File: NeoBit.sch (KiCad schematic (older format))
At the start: 18 parts, among them J2 Barrel_Jack_MountingPin, J5 microbit_edge_connector, U1 74AHCT125, U2 MCP1702-3302E_TO92

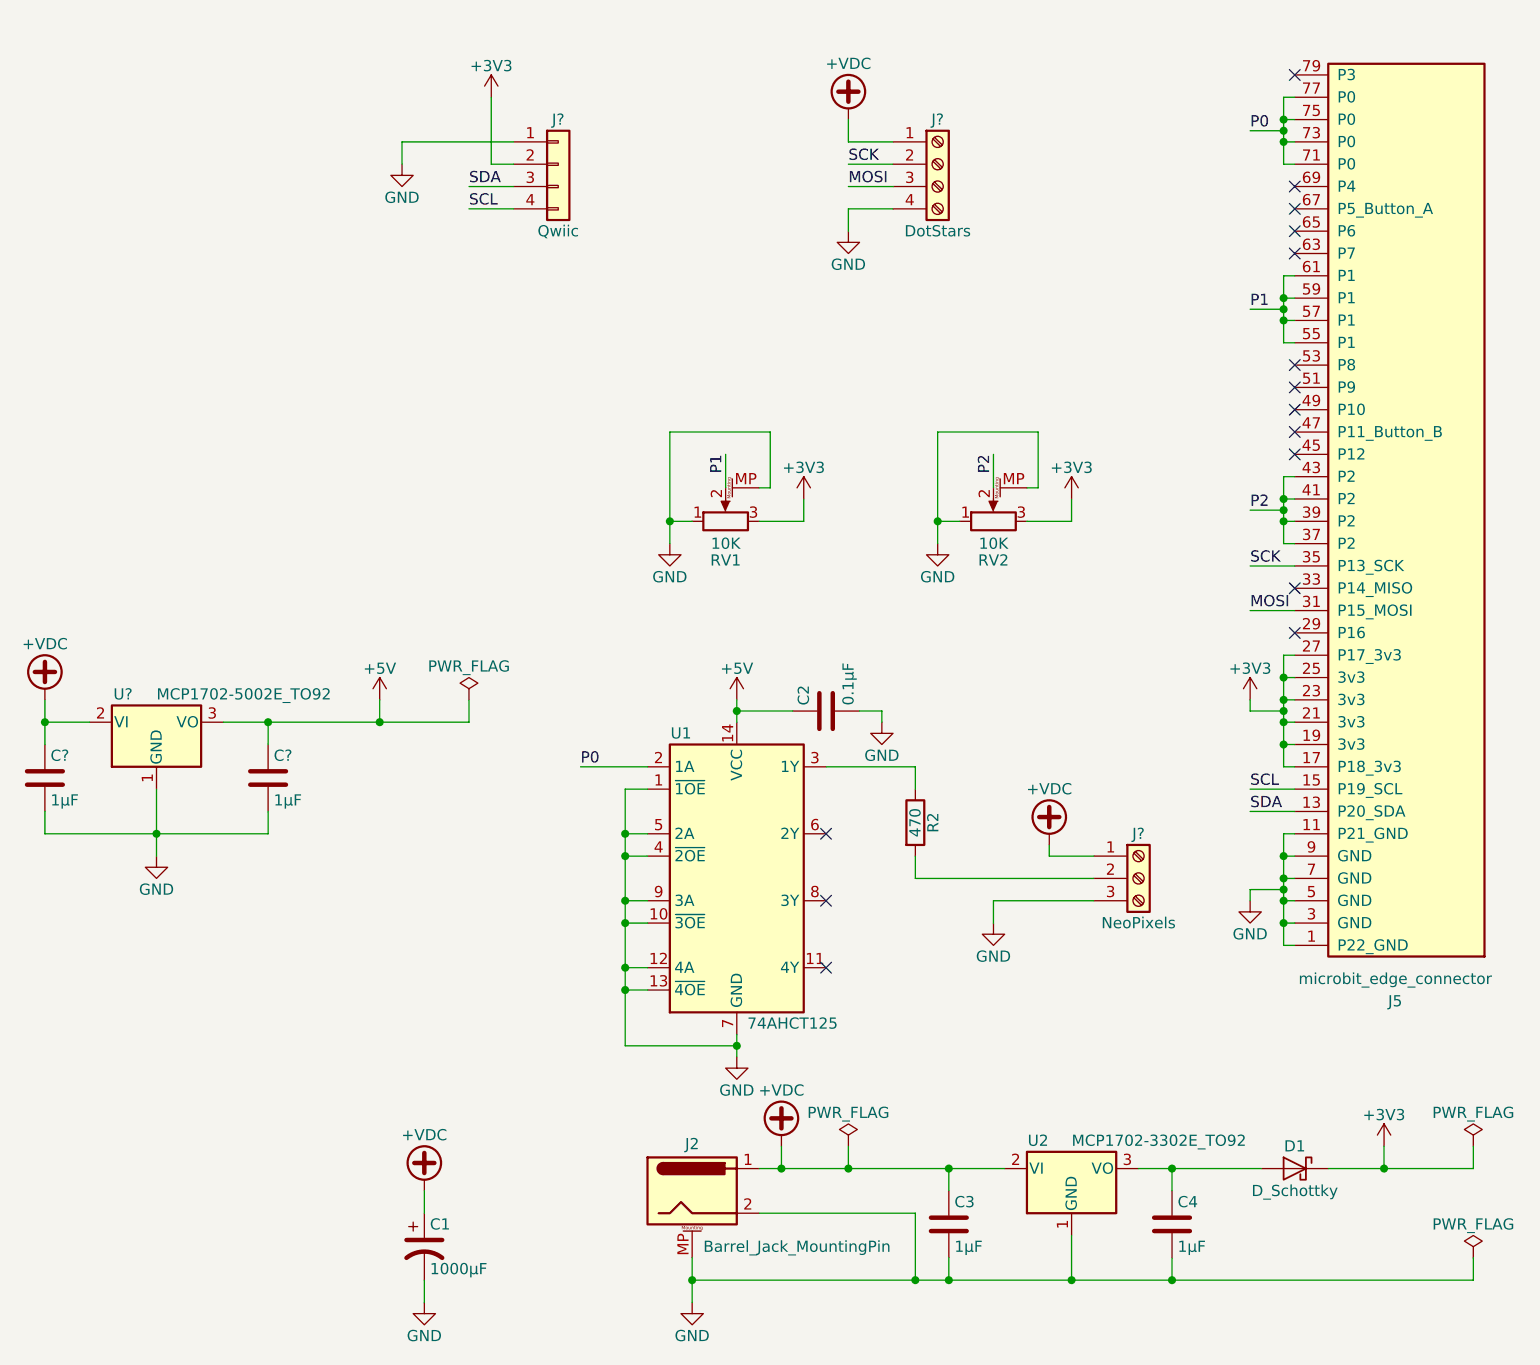
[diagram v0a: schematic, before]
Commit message: Put audio jack on P0; move NeoPixels to P16.
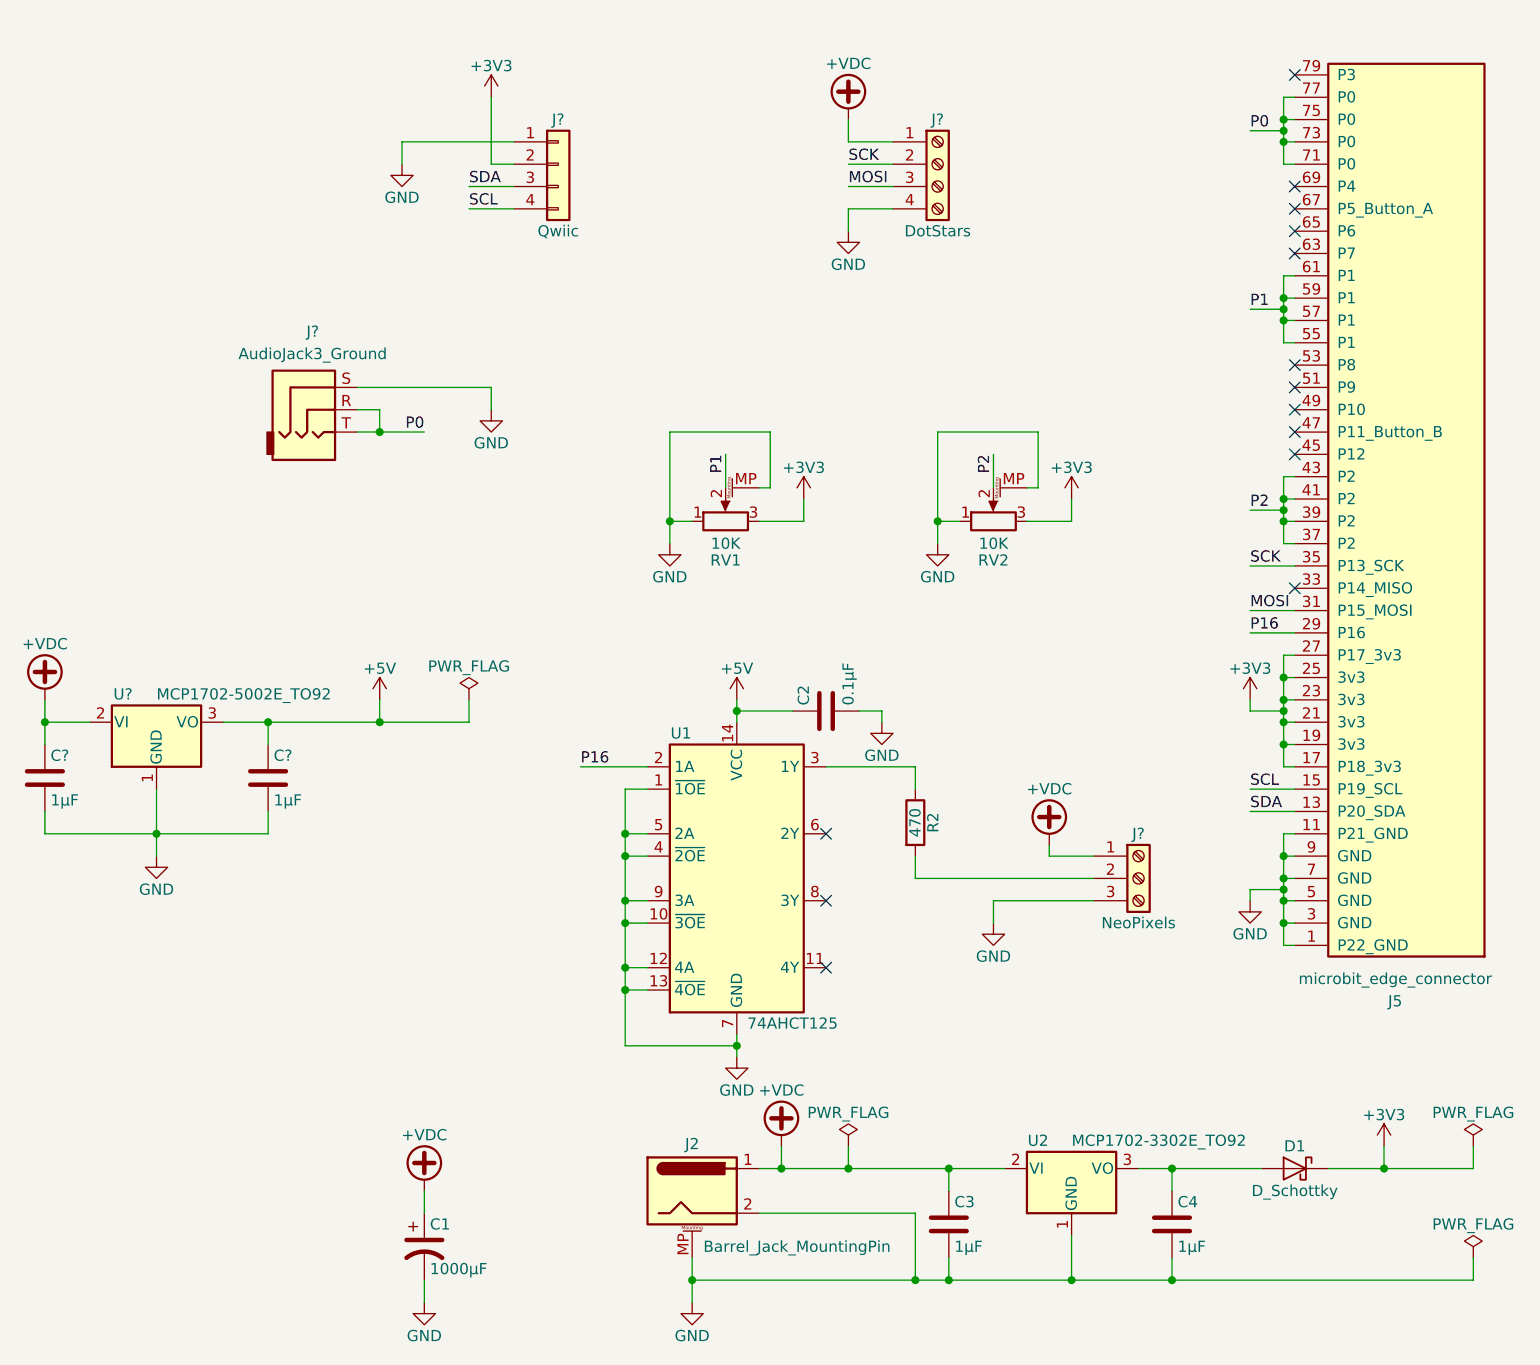
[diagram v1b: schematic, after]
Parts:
- added J?: AudioJack3_Ground, symbol AudioJack3_Ground
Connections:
- net GND: now also J?.S
- net P0: now also J?.R, J?.T; no longer U1.2 (1A)
- net P16: now reaches J5.29 (P16)
- net P16: now also U1.2 (1A)
- no-connect marks 15 -> 14
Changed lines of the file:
@@
 Connection ~ 4200 5300
 Text Label 4000 4300 0    50   ~ 0
-P0
+P16
 Wire Wire Line
 	4000 4300 4300 4300
@@
 NoConn ~ 7200 2900
 NoConn ~ 7200 3500
-NoConn ~ 7200 3700
 Wire Wire Line
 	7600 6000 7600 6100
@@
 Wire Wire Line
 	3500 1800 3700 1800
+$Comp
+L AudioJack3_Ground J?
+U 1 1 5BA405B2
+P 2800 2700
+F 0 "J?" H 2800 3050 50  0000 C CNN
+F 1 "AudioJack3_Ground" H 2800 2950 50  0000 C CNN
+F 2 "" H 2800 2700 50  0001 C CNN
+F 3 "" H 2800 2700 50  0001 C CNN
+	1    2800 2700
+	1    0    0    -1
+$EndComp
+$Comp
+L GND #PWR?
+U 1 1 5BA40629
+P 3600 2700
+F 0 "#PWR?" H 3600 2450 50  0001 C CNN
+F 1 "GND" H 3600 2550 50  0000 C CNN
+F 2 "" H 3600 2700 50  0001 C CNN
+F 3 "" H 3600 2700 50  0001 C CNN
+	1    3600 2700
+	1    0    0    -1
+$EndComp
+Wire Wire Line
+	3000 2600 3600 2600
+Wire Wire Line
+	3600 2600 3600 2700
+Text Label 3300 2800 2    50   ~ 0
+P0
+Wire Wire Line
+	3000 2800 3300 2800
+Wire Wire Line
+	3000 2700 3100 2700
+Wire Wire Line
+	3100 2700 3100 2800
+Connection ~ 3100 2800
+Text Label 7000 3700 0    50   ~ 0
+P16
+Wire Wire Line
+	7000 3700 7200 3700
 $EndSCHEMATC

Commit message: Annotate schematic.
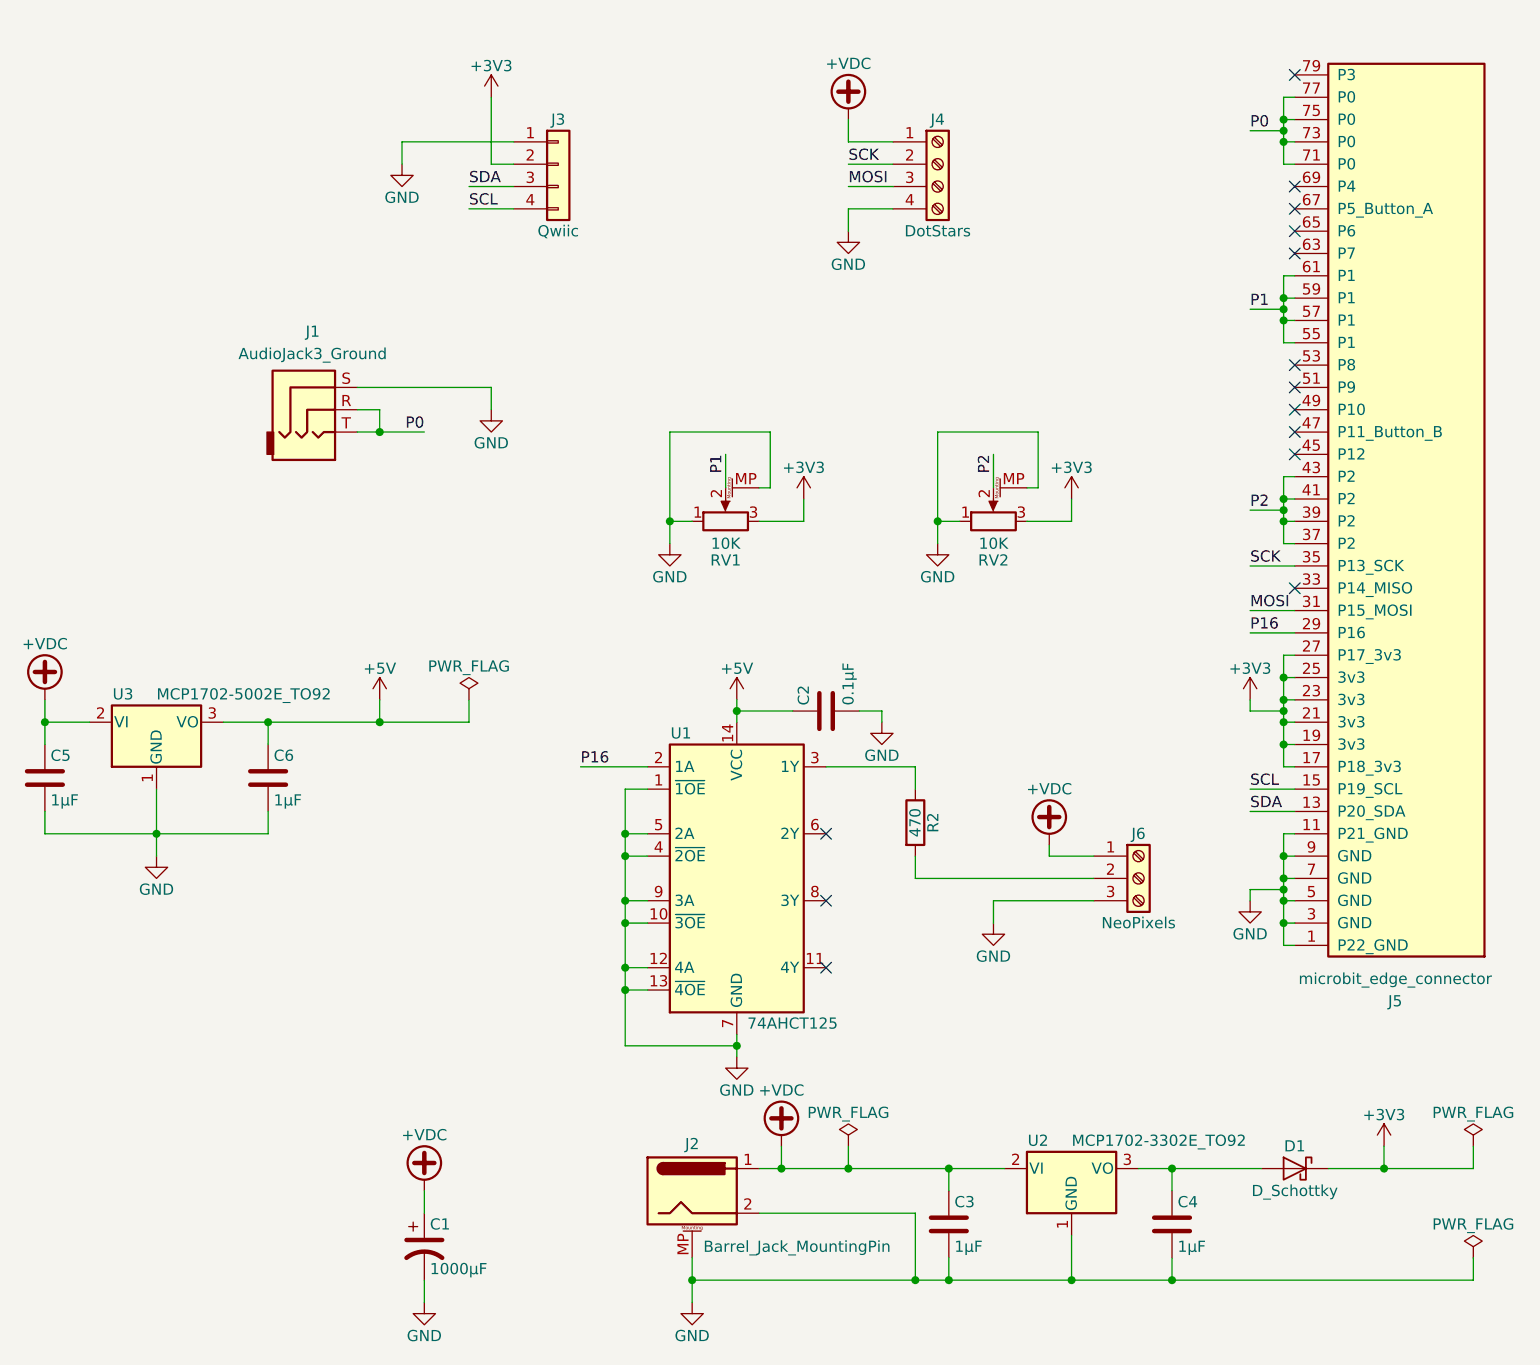
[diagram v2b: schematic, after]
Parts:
- J1: renamed from J?; Description (none) -> CONN JACK STEREO 3.5MM R/A; Digi-Key_PN (none) -> CP1-3523N-ND; MPN (none) -> SJ1-3523N
- gave numbers to parts that had none: 6
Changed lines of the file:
@@
 	4700 5500 4700 5600
 $Comp
-L GND #PWR08
+L GND #PWR07
 U 1 1 5B879F3C
 P 4500 6700
-F 0 "#PWR08" H 4500 6450 50  0001 C CNN
+F 0 "#PWR07" H 4500 6450 50  0001 C CNN
 F 1 "GND" H 4500 6550 50  0000 C CNN
 F 2 "" H 4500 6700 50  0001 C CNN
@@
 Connection ~ 6200 6600
 $Comp
-L +3V3 #PWR09
+L +3V3 #PWR08
 U 1 1 5B87BEFA
 P 7600 6000
-F 0 "#PWR09" H 7600 5850 50  0001 C CNN
+F 0 "#PWR08" H 7600 5850 50  0001 C CNN
 F 1 "+3V3" H 7600 6140 50  0000 C CNN
 F 2 "" H 7600 6000 50  0001 C CNN
@@
 $EndComp
 $Comp
-L GND #PWR010
+L GND #PWR09
 U 1 1 5B87CC46
 P 5350 4100
-F 0 "#PWR010" H 5350 3850 50  0001 C CNN
+F 0 "#PWR09" H 5350 3850 50  0001 C CNN
 F 1 "GND" H 5350 3950 50  0000 C CNN
 F 2 "" H 5350 4100 50  0001 C CNN
@@
 $EndComp
 $Comp
-L GND #PWR011
+L GND #PWR010
 U 1 1 5B87D3B2
 P 3300 6700
-F 0 "#PWR011" H 3300 6450 50  0001 C CNN
+F 0 "#PWR010" H 3300 6450 50  0001 C CNN
 F 1 "GND" H 3300 6550 50  0000 C CNN
 F 2 "" H 3300 6700 50  0001 C CNN
@@
 	3300 6600 3300 6700
 $Comp
-L PWR_FLAG #FLG013
+L PWR_FLAG #FLG011
 U 1 1 5B87DB70
 P 5200 6000
-F 0 "#FLG013" H 5200 6075 50  0001 C CNN
+F 0 "#FLG011" H 5200 6075 50  0001 C CNN
 F 1 "PWR_FLAG" H 5200 6150 50  0000 C CNN
 F 2 "" H 5200 6000 50  0001 C CNN
@@
 $EndComp
 $Comp
-L PWR_FLAG #FLG014
+L PWR_FLAG #FLG012
 U 1 1 5B87DBB4
 P 8000 6000
-F 0 "#FLG014" H 8000 6075 50  0001 C CNN
+F 0 "#FLG012" H 8000 6075 50  0001 C CNN
 F 1 "PWR_FLAG" H 8000 6150 50  0000 C CNN
 F 2 "" H 8000 6000 50  0001 C CNN
@@
 $EndComp
 $Comp
-L PWR_FLAG #FLG015
+L PWR_FLAG #FLG013
 U 1 1 5B87DBF8
 P 8000 6500
-F 0 "#FLG015" H 8000 6575 50  0001 C CNN
+F 0 "#FLG013" H 8000 6575 50  0001 C CNN
 F 1 "PWR_FLAG" H 8000 6650 50  0000 C CNN
 F 2 "" H 8000 6500 50  0001 C CNN
@@
 	4650 3050 4650 2900
 $Comp
-L GND #PWR016
+L GND #PWR014
 U 1 1 5B8B1B29
 P 4400 3300
-F 0 "#PWR016" H 4400 3050 50  0001 C CNN
+F 0 "#PWR014" H 4400 3050 50  0001 C CNN
 F 1 "GND" H 4400 3150 50  0000 C CNN
 F 2 "" H 4400 3300 50  0001 C CNN
@@
 Connection ~ 4400 3200
 $Comp
-L +3V3 #PWR017
+L +3V3 #PWR015
 U 1 1 5B8B1C95
 P 5000 3100
-F 0 "#PWR017" H 5000 2950 50  0001 C CNN
+F 0 "#PWR015" H 5000 2950 50  0001 C CNN
 F 1 "+3V3" H 5000 3240 50  0000 C CNN
 F 2 "" H 5000 3100 50  0001 C CNN
@@
 	5850 3050 5850 2900
 $Comp
-L GND #PWR018
+L GND #PWR016
 U 1 1 5B8B259B
 P 5600 3300
-F 0 "#PWR018" H 5600 3050 50  0001 C CNN
+F 0 "#PWR016" H 5600 3050 50  0001 C CNN
 F 1 "GND" H 5600 3150 50  0000 C CNN
 F 2 "" H 5600 3300 50  0001 C CNN
@@
 Connection ~ 5600 3200
 $Comp
-L +3V3 #PWR019
+L +3V3 #PWR017
 U 1 1 5B8B25A7
 P 6200 3100
-F 0 "#PWR019" H 6200 2950 50  0001 C CNN
+F 0 "#PWR017" H 6200 2950 50  0001 C CNN
 F 1 "+3V3" H 6200 3240 50  0000 C CNN
 F 2 "" H 6200 3100 50  0001 C CNN
@@
 	7600 6000 7600 6100
 $Comp
-L +VDC #PWR?
+L +VDC #PWR018
 U 1 1 5BA32D90
 P 3300 6200
-F 0 "#PWR?" H 3300 6100 50  0001 C CNN
+F 0 "#PWR018" H 3300 6100 50  0001 C CNN
 F 1 "+VDC" H 3300 6450 50  0000 C CNN
 F 2 "" H 3300 6200 50  0001 C CNN
@@
 $EndComp
 $Comp
-L +VDC #PWR?
+L +VDC #PWR019
 U 1 1 5BA32FD2
 P 6100 4650
-F 0 "#PWR?" H 6100 4550 50  0001 C CNN
+F 0 "#PWR019" H 6100 4550 50  0001 C CNN
 F 1 "+VDC" H 6100 4900 50  0000 C CNN
 F 2 "" H 6100 4650 50  0001 C CNN
@@
 $EndComp
 $Comp
-L +VDC #PWR?
+L +VDC #PWR020
 U 1 1 5BA33004
 P 4900 6000
-F 0 "#PWR?" H 4900 5900 50  0001 C CNN
+F 0 "#PWR020" H 4900 5900 50  0001 C CNN
 F 1 "+VDC" H 4900 6250 50  0000 C CNN
 F 2 "" H 4900 6000 50  0001 C CNN
@@
 $EndComp
 $Comp
-L MCP1700-5002E_TO92 U?
+L MCP1700-5002E_TO92 U3
 U 1 1 5BA331CB
 P 2100 4100
-F 0 "U?" H 1950 3975 50  0000 C CNN
+F 0 "U3" H 1950 3975 50  0000 C CNN
 F 1 "MCP1702-5002E_TO92" H 2100 3975 50  0000 L CNN
 F 2 "TO_SOT_Packages_THT:TO-92_Inline_Narrow_Oval" H 2100 3900 50  0001 C CIN
@@
 $EndComp
 $Comp
-L C C?
+L C C5
 U 1 1 5BA3332C
 P 1600 4350
-F 0 "C?" H 1625 4450 50  0000 L CNN
+F 0 "C5" H 1625 4450 50  0000 L CNN
 F 1 "1µF" H 1625 4250 50  0000 L CNN
 F 2 "Capacitors_THT:C_Rect_L7.0mm_W2.5mm_P5.00mm" H 1638 4200 50  0001 C CNN
@@
 $EndComp
 $Comp
-L C C?
+L C C6
 U 1 1 5BA3337C
 P 2600 4350
-F 0 "C?" H 2625 4450 50  0000 L CNN
+F 0 "C6" H 2625 4450 50  0000 L CNN
 F 1 "1µF" H 2625 4250 50  0000 L CNN
 F 2 "Capacitors_THT:C_Rect_L7.0mm_W2.5mm_P5.00mm" H 2638 4200 50  0001 C CNN
@@
 $EndComp
 $Comp
-L +VDC #PWR?
+L +VDC #PWR021
 U 1 1 5BA3347F
 P 1600 4000
-F 0 "#PWR?" H 1600 3900 50  0001 C CNN
+F 0 "#PWR021" H 1600 3900 50  0001 C CNN
 F 1 "+VDC" H 1600 4250 50  0000 C CNN
 F 2 "" H 1600 4000 50  0001 C CNN
@@
 $EndComp
 $Comp
-L GND #PWR?
+L GND #PWR022
 U 1 1 5BA33626
 P 2100 4700
-F 0 "#PWR?" H 2100 4450 50  0001 C CNN
+F 0 "#PWR022" H 2100 4450 50  0001 C CNN
 F 1 "GND" H 2100 4550 50  0000 C CNN
 F 2 "" H 2100 4700 50  0001 C CNN
@@
 Connection ~ 2100 4600
 $Comp
-L PWR_FLAG #FLG?
+L PWR_FLAG #FLG023
 U 1 1 5BA33AB3
 P 3500 4000
-F 0 "#FLG?" H 3500 4075 50  0001 C CNN
+F 0 "#FLG023" H 3500 4075 50  0001 C CNN
 F 1 "PWR_FLAG" H 3500 4150 50  0000 C CNN
 F 2 "" H 3500 4000 50  0001 C CNN
@@
 Connection ~ 3100 4100
 $Comp
-L Screw_Terminal_01x03 J?
+L Screw_Terminal_01x03 J6
 U 1 1 5BA3E89A
 P 6500 4800
-F 0 "J?" H 6500 5000 50  0000 C CNN
+F 0 "J6" H 6500 5000 50  0000 C CNN
 F 1 "NeoPixels" H 6500 4600 50  0000 C CNN
 F 2 "" H 6500 4800 50  0001 C CNN
@@
 	7000 4500 7200 4500
 $Comp
-L Screw_Terminal_01x04 J?
+L Screw_Terminal_01x04 J4
 U 1 1 5BA3F768
 P 5600 1600
-F 0 "J?" H 5600 1800 50  0000 C CNN
+F 0 "J4" H 5600 1800 50  0000 C CNN
 F 1 "DotStars" H 5600 1300 50  0000 C CNN
 F 2 "" H 5600 1600 50  0001 C CNN
@@
 $EndComp
 $Comp
-L +VDC #PWR?
+L +VDC #PWR024
 U 1 1 5BA4005E
 P 5200 1400
-F 0 "#PWR?" H 5200 1300 50  0001 C CNN
+F 0 "#PWR024" H 5200 1300 50  0001 C CNN
 F 1 "+VDC" H 5200 1650 50  0000 C CNN
 F 2 "" H 5200 1400 50  0001 C CNN
@@
 $EndComp
 $Comp
-L GND #PWR?
+L GND #PWR025
 U 1 1 5BA4009C
 P 5200 1900
-F 0 "#PWR?" H 5200 1650 50  0001 C CNN
+F 0 "#PWR025" H 5200 1650 50  0001 C CNN
 F 1 "GND" H 5200 1750 50  0000 C CNN
 F 2 "" H 5200 1900 50  0001 C CNN
@@
 	5200 1700 5400 1700
 $Comp
-L Conn_01x04 J?
+L Conn_01x04 J3
 U 1 1 5BA3FCC1
 P 3900 1600
-F 0 "J?" H 3900 1800 50  0000 C CNN
+F 0 "J3" H 3900 1800 50  0000 C CNN
 F 1 "Qwiic" H 3900 1300 50  0000 C CNN
 F 2 "" H 3900 1600 50  0001 C CNN
@@
 $EndComp
 $Comp
-L GND #PWR?
+L GND #PWR026
 U 1 1 5BA3FE93
 P 3200 1600
-F 0 "#PWR?" H 3200 1350 50  0001 C CNN
+F 0 "#PWR026" H 3200 1350 50  0001 C CNN
 F 1 "GND" H 3200 1450 50  0000 C CNN
 F 2 "" H 3200 1600 50  0001 C CNN
@@
 	3200 1500 3700 1500
 $Comp
-L +3V3 #PWR?
+L +3V3 #PWR027
 U 1 1 5BA3FF8D
 P 3600 1300
-F 0 "#PWR?" H 3600 1150 50  0001 C CNN
+F 0 "#PWR027" H 3600 1150 50  0001 C CNN
 F 1 "+3V3" H 3600 1440 50  0000 C CNN
 F 2 "" H 3600 1300 50  0001 C CNN
@@
 	3500 1800 3700 1800
 $Comp
-L AudioJack3_Ground J?
+L AudioJack3_Ground J1
 U 1 1 5BA405B2
 P 2800 2700
-F 0 "J?" H 2800 3050 50  0000 C CNN
+F 0 "J1" H 2800 3050 50  0000 C CNN
 F 1 "AudioJack3_Ground" H 2800 2950 50  0000 C CNN
 F 2 "" H 2800 2700 50  0001 C CNN
 F 3 "" H 2800 2700 50  0001 C CNN
+F 4 "SJ1-3523N" H 2800 2700 60  0001 C CNN "MPN"
+F 5 "CONN JACK STEREO 3.5MM R/A" H 2800 2700 60  0001 C CNN "Description"
+F 6 "CP1-3523N-ND" H 2800 2700 60  0001 C CNN "Digi-Key_PN"
 	1    2800 2700
 	1    0    0    -1
 $EndComp
 $Comp
-L GND #PWR?
+L GND #PWR028
 U 1 1 5BA40629
 P 3600 2700
-F 0 "#PWR?" H 3600 2450 50  0001 C CNN
+F 0 "#PWR028" H 3600 2450 50  0001 C CNN
 F 1 "GND" H 3600 2550 50  0000 C CNN
 F 2 "" H 3600 2700 50  0001 C CNN
